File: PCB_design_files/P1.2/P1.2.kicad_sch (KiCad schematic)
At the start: 37 parts, among them J1 -EEG_INPUT, J2 +EEG_INPUT, J3 +3.3V, J4 GND, J5 -3V3, J6 EEG_INPUT, J7 STAGE_1_OUT, J8 STAGE_2_OUT, J9 STAGE_3_OUT, U1 INA819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

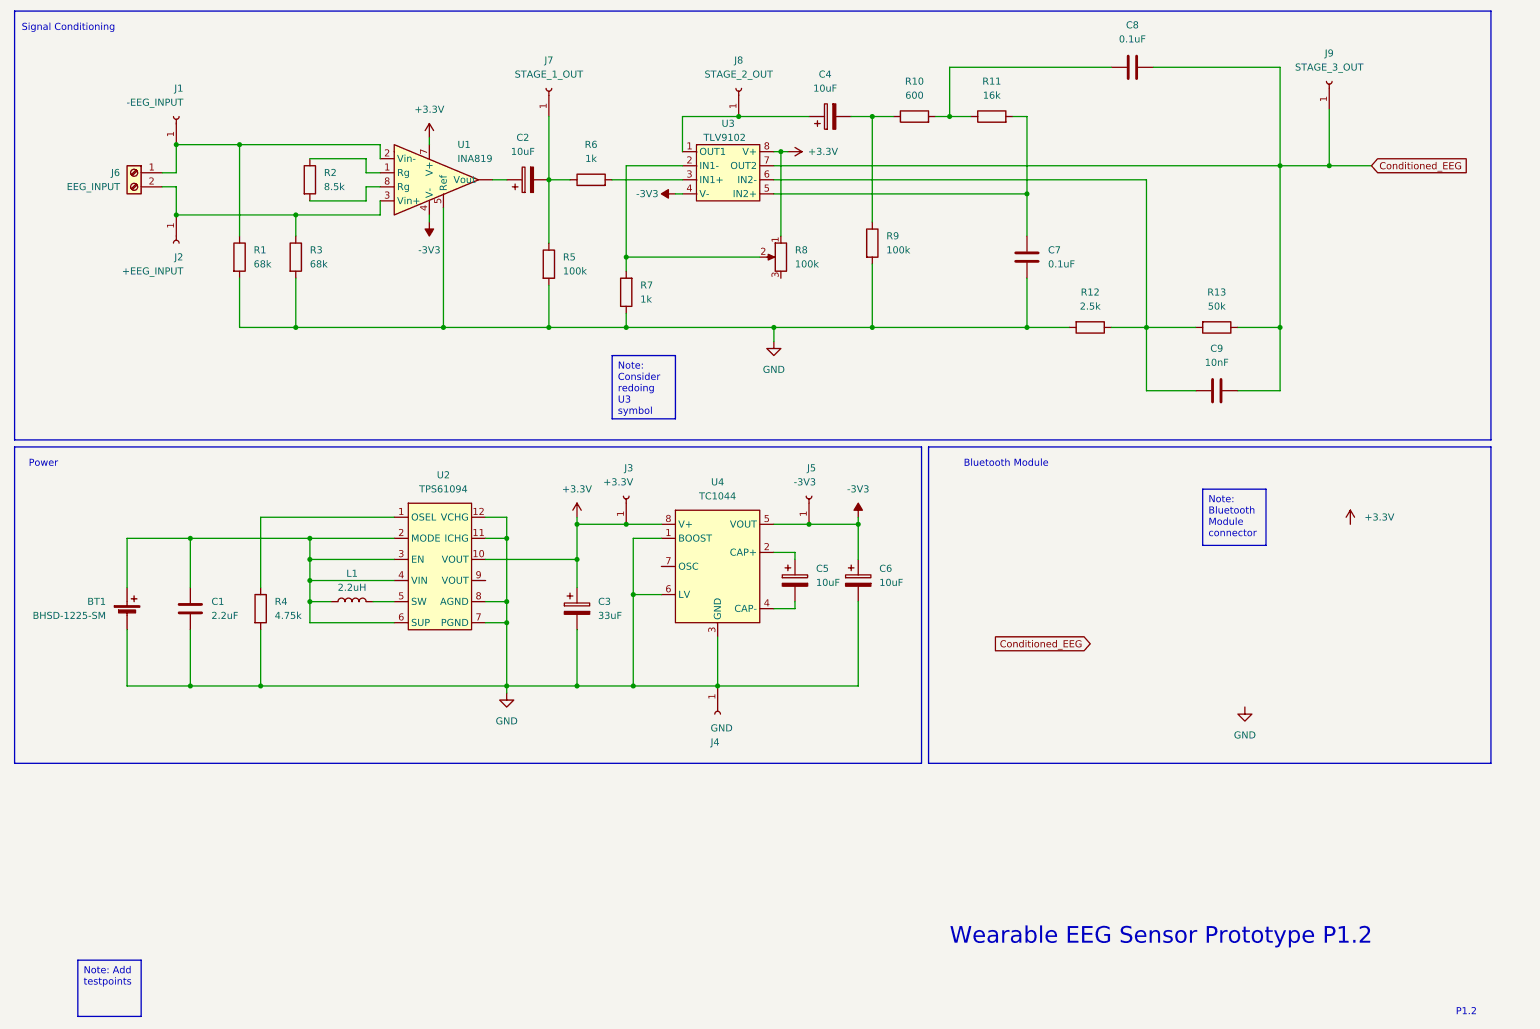
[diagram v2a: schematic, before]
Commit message: Fixed some symbols. Started PCB layout
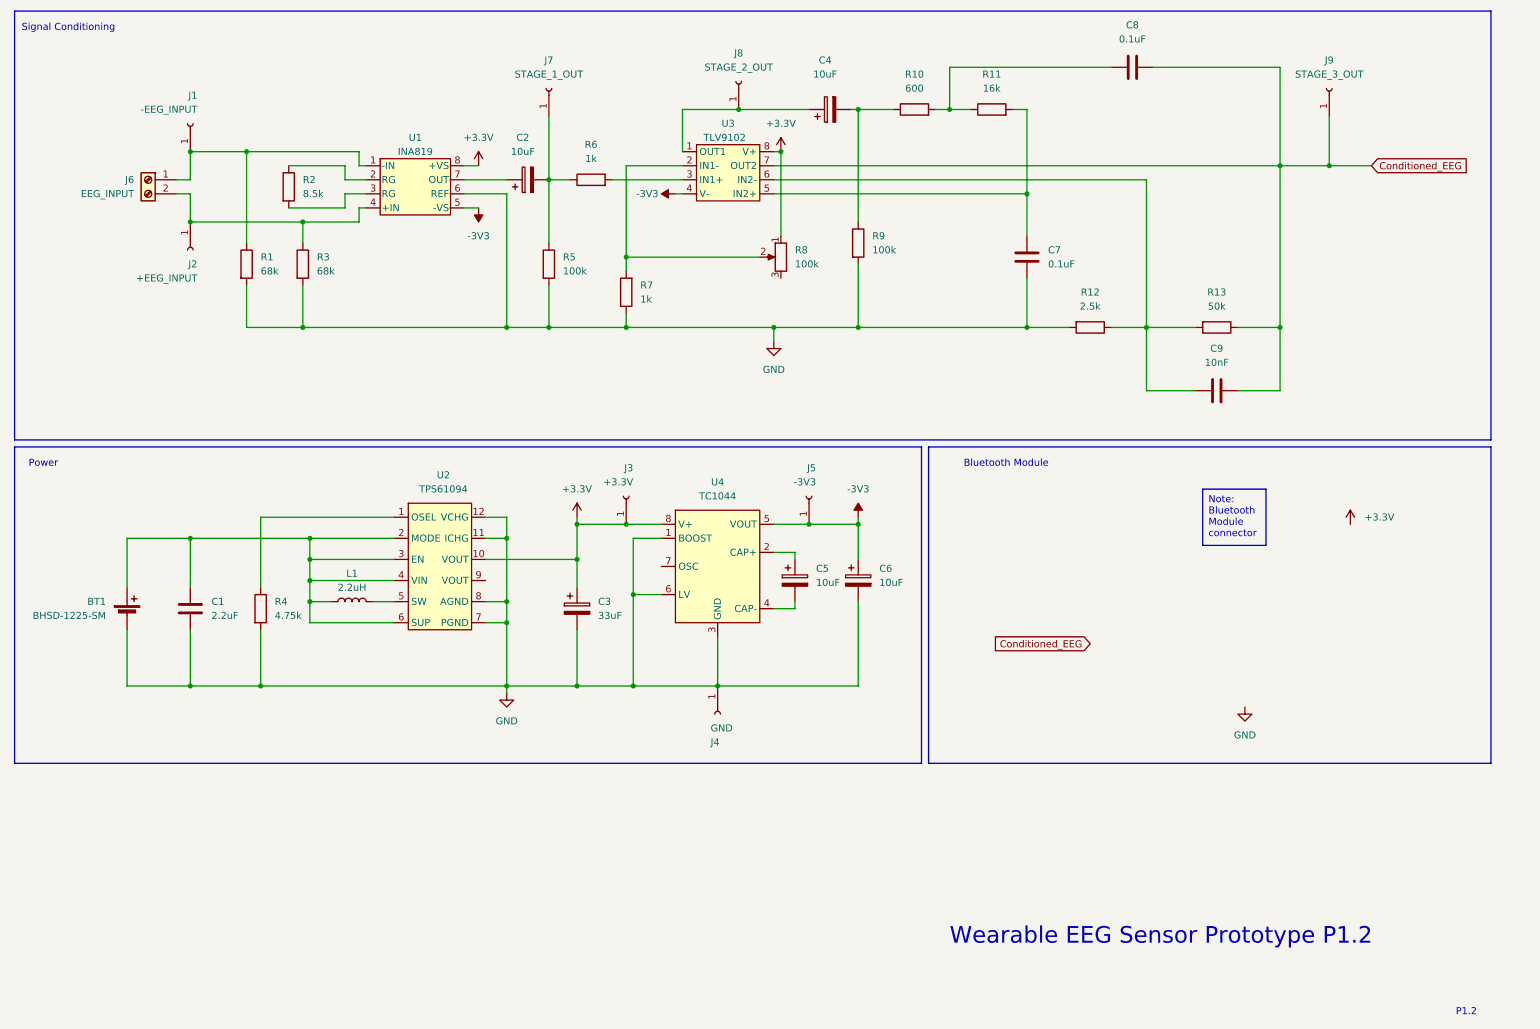
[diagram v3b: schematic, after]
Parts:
- R8: footprint Resistor_THT:R_Axial_DIN0207_L6.3mm_D2.5mm_P10.16mm_Horizontal -> Potentiometer_THT:Potentiometer_Bourns_3296W_Vertical
- U1: symbol My_Library:INA118 -> INA819ID:INA819ID
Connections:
- net +3.3V: now also U1.8 (+VS); no longer U1.7 (V+)
- net -3V3: now also U1.5 (-VS); no longer U1.4 (V-)
- net GND: now also U1.6 (REF); no longer U1.5 (Ref)
- net at C2.1: now also U1.7 (OUT); no longer U1. (Vout)
- net at U1.1 (-IN): now also J1.1 (Pin_1), J6.1 (Pin_1), R1.1; no longer R2.1
- net at J2.1 (Pin_1), J6.2 (Pin_2), R3.1: now also U1.4 (+IN); no longer U1.3 (Vin+)
- net at R2.2: now also U1.3 (RG); no longer U1.8 (Rg)
- new net: R2.1, U1.2 (RG)
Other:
- moved on the sheet: C4, J1, J2, J6, J8, J9, R1, R10, R11, R2, R3, R9

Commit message: fixed some IC symbols
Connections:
- net -3V3: now also C6.2; no longer C6.1
- net GND: now also C6.1; no longer C6.2
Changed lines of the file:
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@@
     (fill (type none))
+  )
+  (text_box "1044 is backwards"
+    (at 137.16 167.64 0) (size 11.43 10.16)
+    (stroke (width 0) (type default))
+    (fill (type color) (color 255 215 209 1))
+    (effects (font (size 1.27 1.27)) (justify left top))
   )
   (text_box "Note: Bluetooth Module connector"
@@
     )
   )
-  (symbol (lib_id "Device:C_Polarized") (at 165.1 115.57 0) (unit 1)
-    (in_bom yes) (on_board yes) (dnp no) (fields_autoplaced)
-    (property "Reference" "C6" (at 168.91 113.411 0)
-      (effects (font (size 1.27 1.27)) (justify left))
-    )
-    (property "Value" "10uF" (at 168.91 115.951 0)
-      (effects (font (size 1.27 1.27)) (justify left))
-    )
-    (property "Footprint" "Capacitor_THT:CP_Radial_D5.0mm_P2.50mm" (at 166.0652 119.38 0)
-      (effects (font (size 1.27 1.27)) hide)
-    )
+  (symbol (lib_id "Device:C_Polarized") (at 165.1 115.57 0) (mirror x) (unit 1)
+    (in_bom yes) (on_board yes) (dnp no)
+    (property "Reference" "C6" (at 168.91 117.729 0)
+      (effects (font (size 1.27 1.27)) (justify left))
+    )
+    (property "Value" "10uF" (at 168.91 115.189 0)
+      (effects (font (size 1.27 1.27)) (justify left))
+    )
+    (property "Footprint" "Capacitor_THT:CP_Radial_D5.0mm_P2.50mm" (at 166.0652 111.76 0)
+      (effects (font (size 1.27 1.27)) hide)
+    )

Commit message: Created PCB Layout
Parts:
- added J10: BAT+, TestPoint:TestPoint_Loop_D2.50mm_Drill1.0mm, symbol Connector:Conn_01x01_Socket
- added J11: BOOST, TestPoint:TestPoint_Loop_D2.50mm_Drill1.0mm, symbol Connector:Conn_01x01_Socket
- J1: value -EEG_INPUT -> EEG_IN-
- J2: value +EEG_INPUT -> EEG_IN+
- R13: value 50k -> 100k
- U4: value TC1044 -> TC1044S
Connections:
- net +3.3V: no longer R8.1
- net Conditioned_EEG: now also R8.2; no longer R13.1
- net GND: no longer U4.1 (BOOST)
- net at C9.2, R12.1, U3.6 (IN2-): now also R8.1; no longer R13.2
- net STAGE_2_OUT: now reaches C4.1, J8.1 (Pin_1), U3.1 (OUT1)
- net STAGE_2_OUT: now also R13.1
- net STAGE_1_OUT: now reaches C2.2, J7.1 (Pin_1), R5.1, R6.1
- net EEG_IN-: now reaches J1.1 (Pin_1), J6.1 (EEG_IN-), R1.1, U1.1 (IN-)
- net EEG_IN+: now reaches J2.1 (Pin_1), J6.2 (EEG_IN-), R3.1, U1.4 (IN+)
- net BAT+: now reaches BT1.1 (+), C1.1, L1.1, U2.2 (MODE), U2.3 (EN), U2.4 (VIN), U2.6 (SUP)
- net BAT+: now also J10.1 (Pin_1)
- net at R7.2, U3.2 (IN1-): now also R13.2; no longer R8.2
- new net: J11.1 (Pin_1), U4.1 (BOOST)
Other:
- note added: "Power: Test Pins"
- note added: "Signal Conditioning: Test Pins"
- moved on the sheet: BT1, C1, C2, C3, C4, C5, C6, C7, C8, C9, J1, J2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

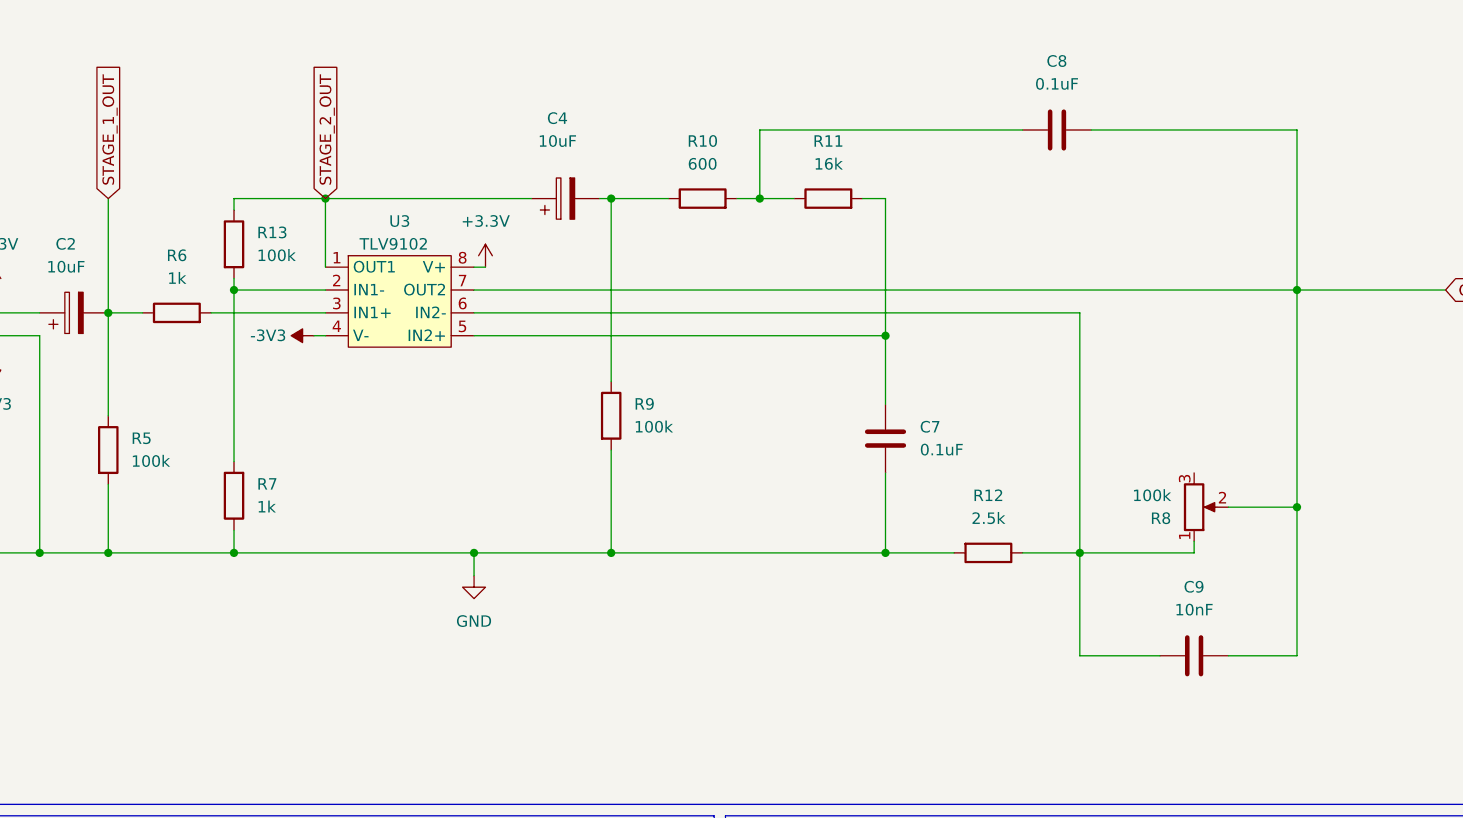
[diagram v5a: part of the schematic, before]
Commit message: swapped R13 and R8
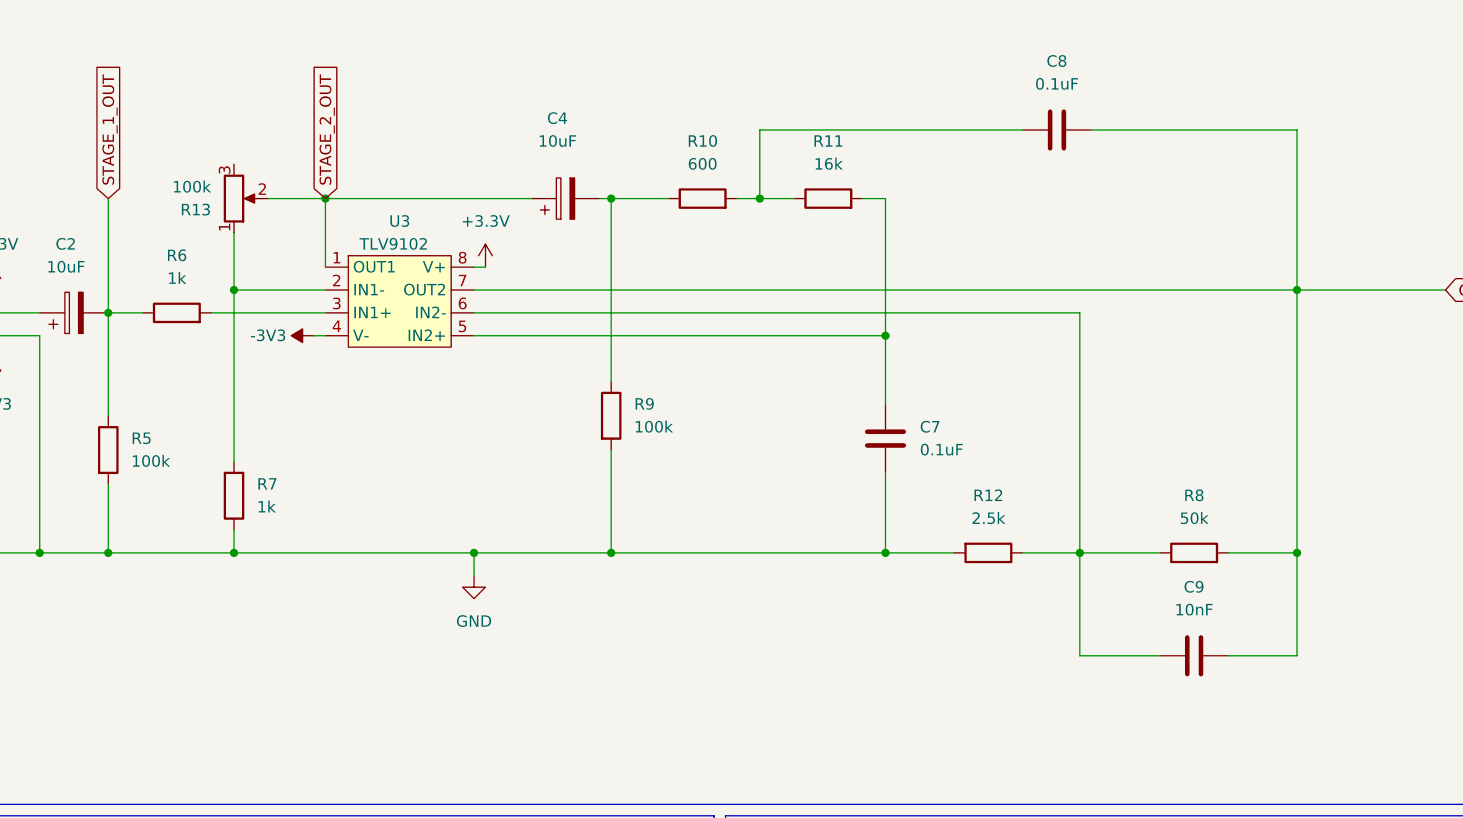
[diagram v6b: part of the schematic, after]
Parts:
- removed R13: 100k, Resistor_THT:R_Axial_DIN0207_L6.3mm_D2.5mm_P10.16mm_Horizontal, symbol Device:R
- removed R8: 100k, Potentiometer_THT:Potentiometer_Bourns_3296W_Vertical, symbol Device:R_Potentiometer
- added R13: 100k, Potentiometer_THT:Potentiometer_Bourns_3296W_Vertical, symbol Device:R_Potentiometer
- added R8: 50k, Resistor_THT:R_Axial_DIN0207_L6.3mm_D2.5mm_P10.16mm_Horizontal, symbol Device:R
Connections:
- net Conditioned_EEG: now also R8.2
- net STAGE_2_OUT: now also R13.2
- net at C9.2, R12.1, U3.6 (IN2-): now also R8.1
- net at R7.2, U3.2 (IN1-): now also R13.1

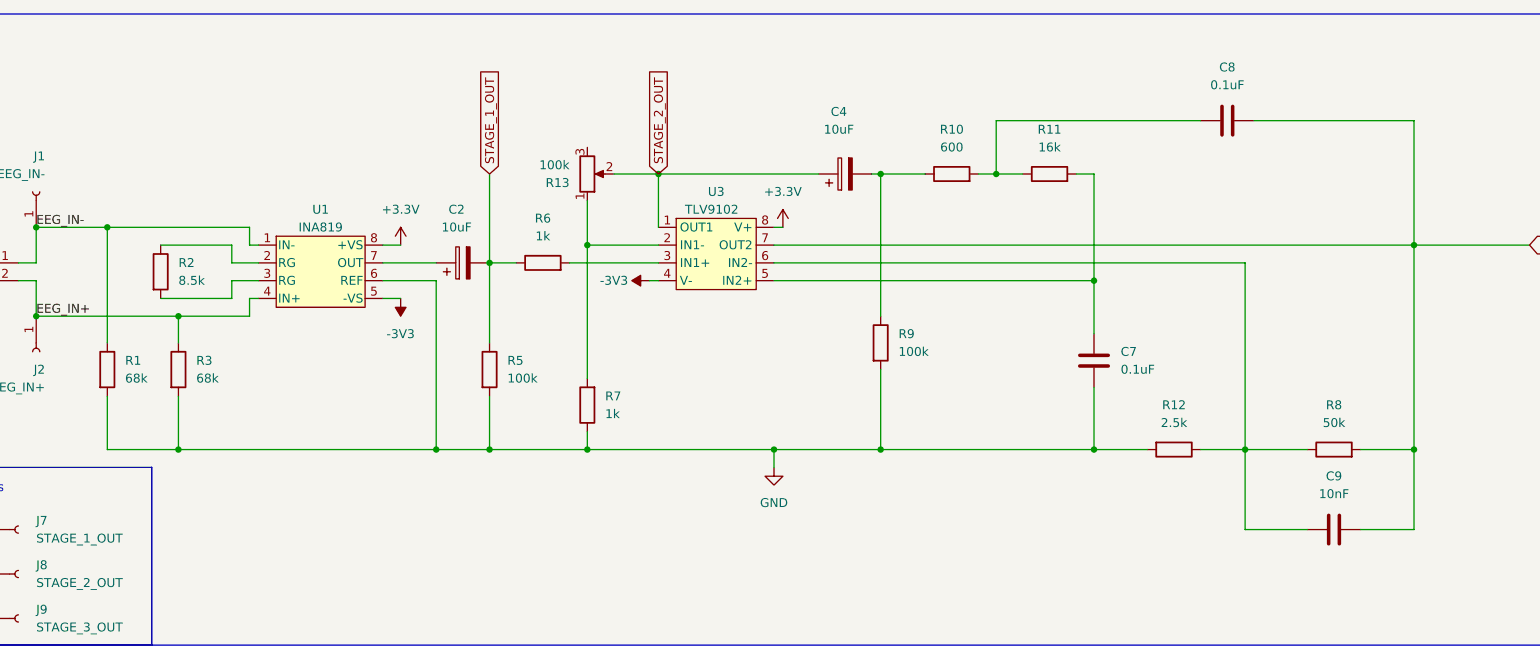
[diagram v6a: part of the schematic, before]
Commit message: Resistor values should now match those purchased
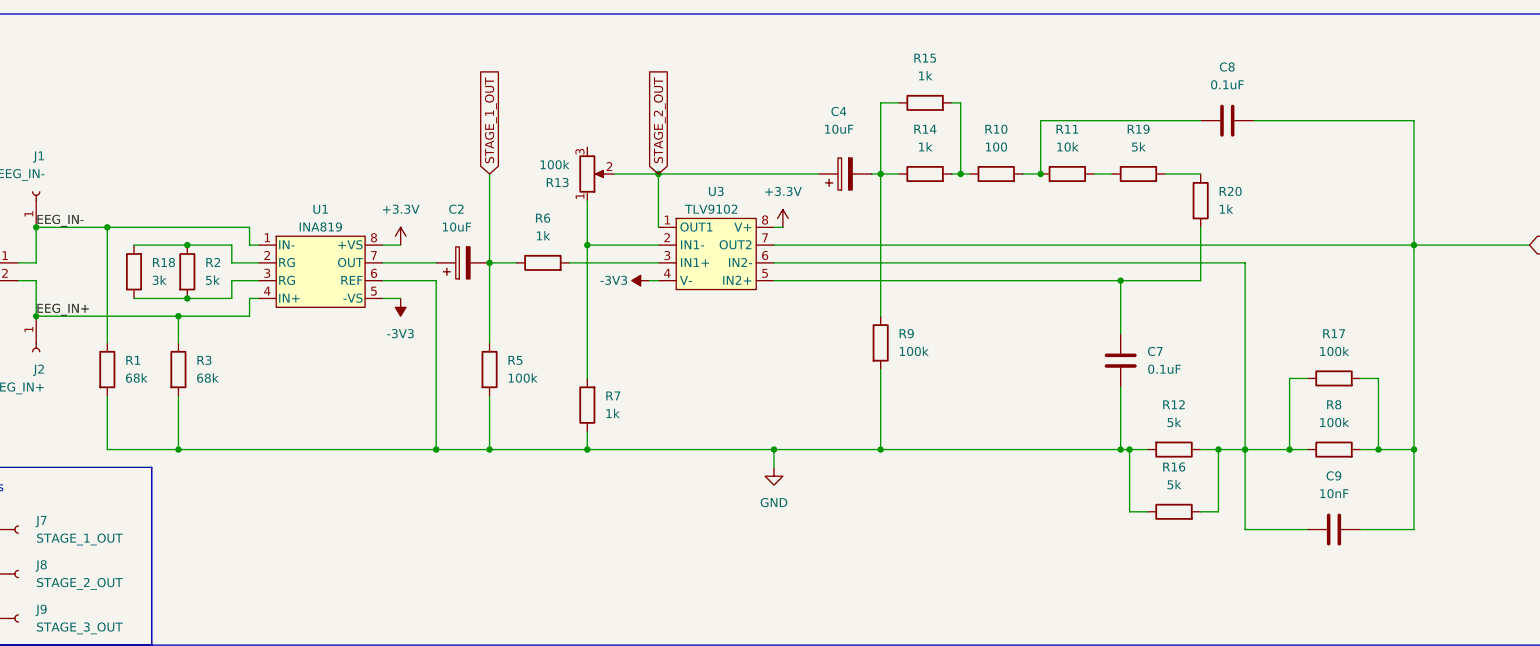
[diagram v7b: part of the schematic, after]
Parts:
- added R14, R15, R20: 1k, symbol Device:R
- added R16, R19: 5k, symbol Device:R
- added R17: 100k, symbol Device:R
- added R18: 3k, symbol Device:R
- R10: value 600 -> 100
- R11: value 16k -> 10k
- R12: value 2.5k -> 5k
- R2: value 8.5k -> 5k
- R8: value 50k -> 100k
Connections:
- net Conditioned_EEG: now also R17.2
- net GND: now also R16.1
- net at C9.2, R12.1, R8.1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: now also R16.2, R17.1
- net at C7.2, U3.5 (IN2+): now also R20.2; no longer R11.2
- net at C4.2, R9.1: now also R14.1, R15.1; no longer R10.1
- net at R2.1, U1.2 (RG): now also R18.2
- net at R2.2, U1.3 (RG): now also R18.1
- new net: R11.2, R19.1
- new net: R10.1, R14.2, R15.2
- new net: R19.2, R20.1
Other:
- moved on the sheet: C7, R10, R11, R2
